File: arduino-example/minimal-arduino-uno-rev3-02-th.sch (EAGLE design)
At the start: 15 parts, among them J1 3x2 M, J3 POWERSUPPLY_DC21MMX, U1 NCP1117ST50T3G, X1 CSTCE16M0V53-R0 16MHZ

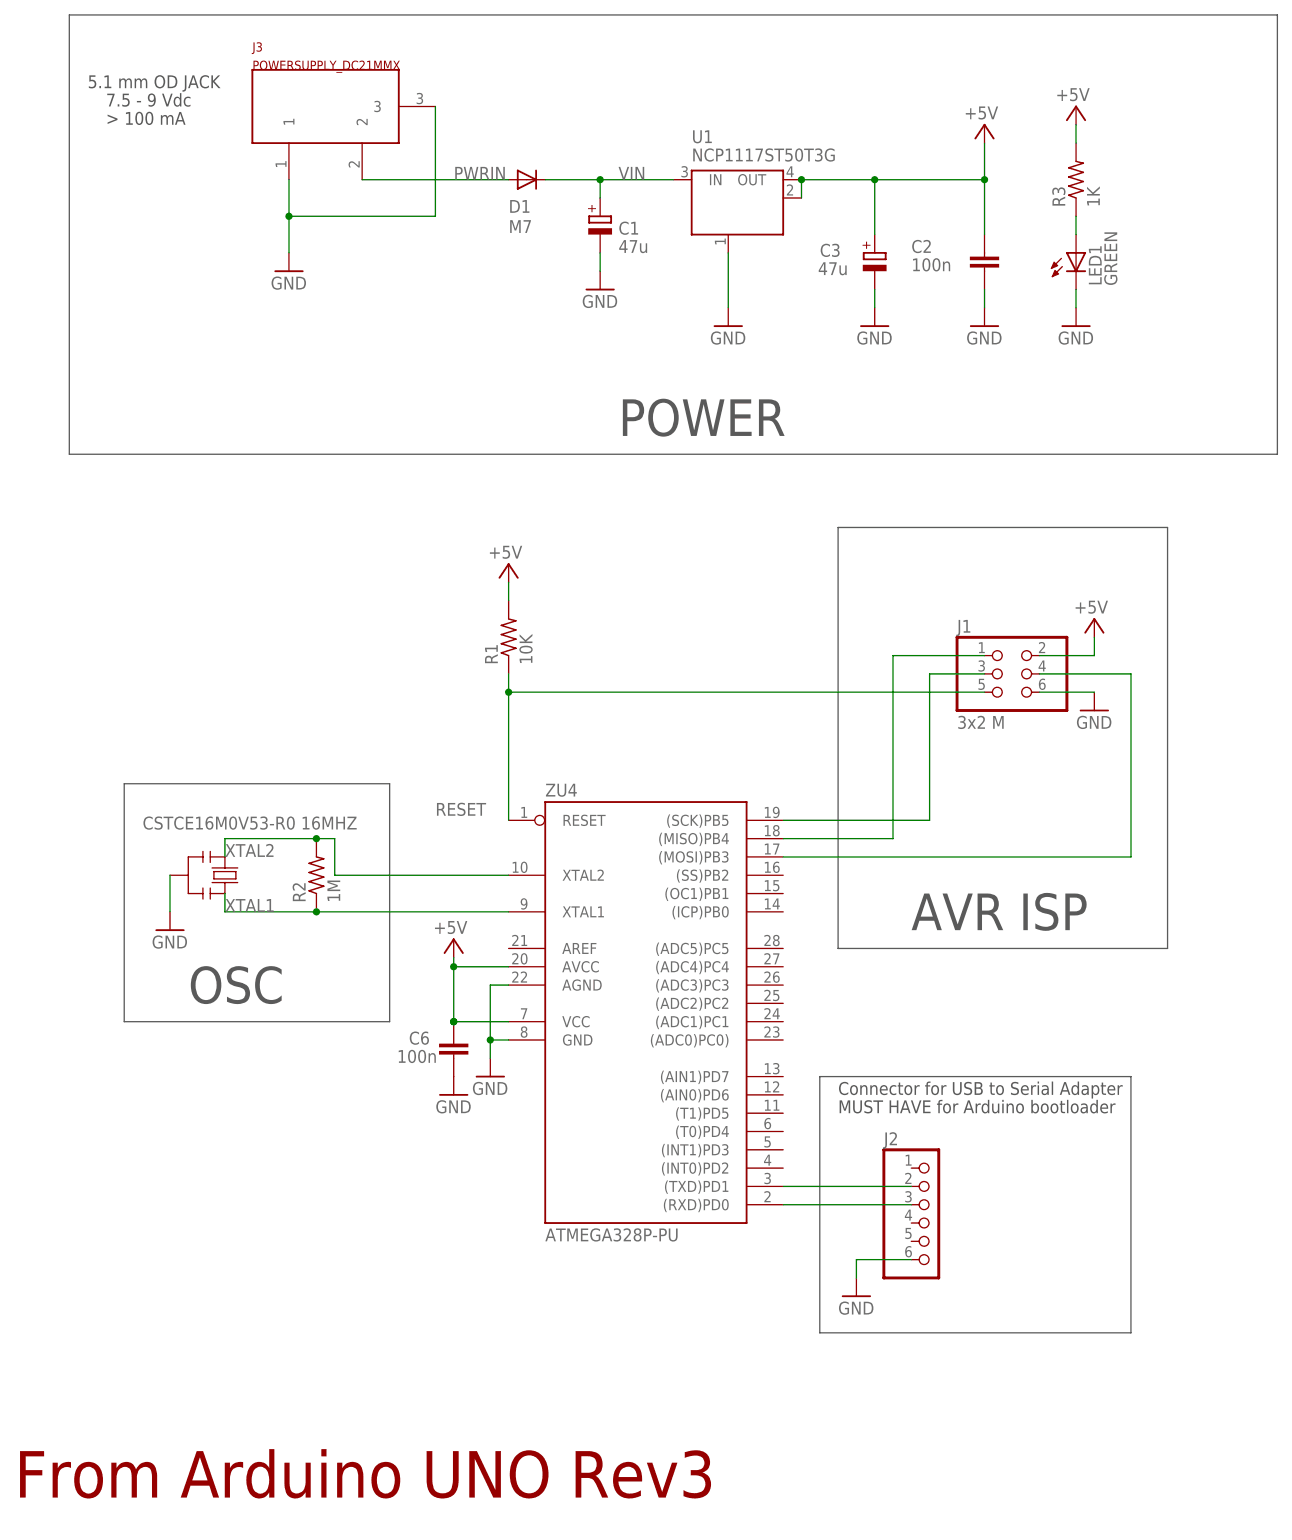
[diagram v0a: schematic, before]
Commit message: Updated minimal arduino board.
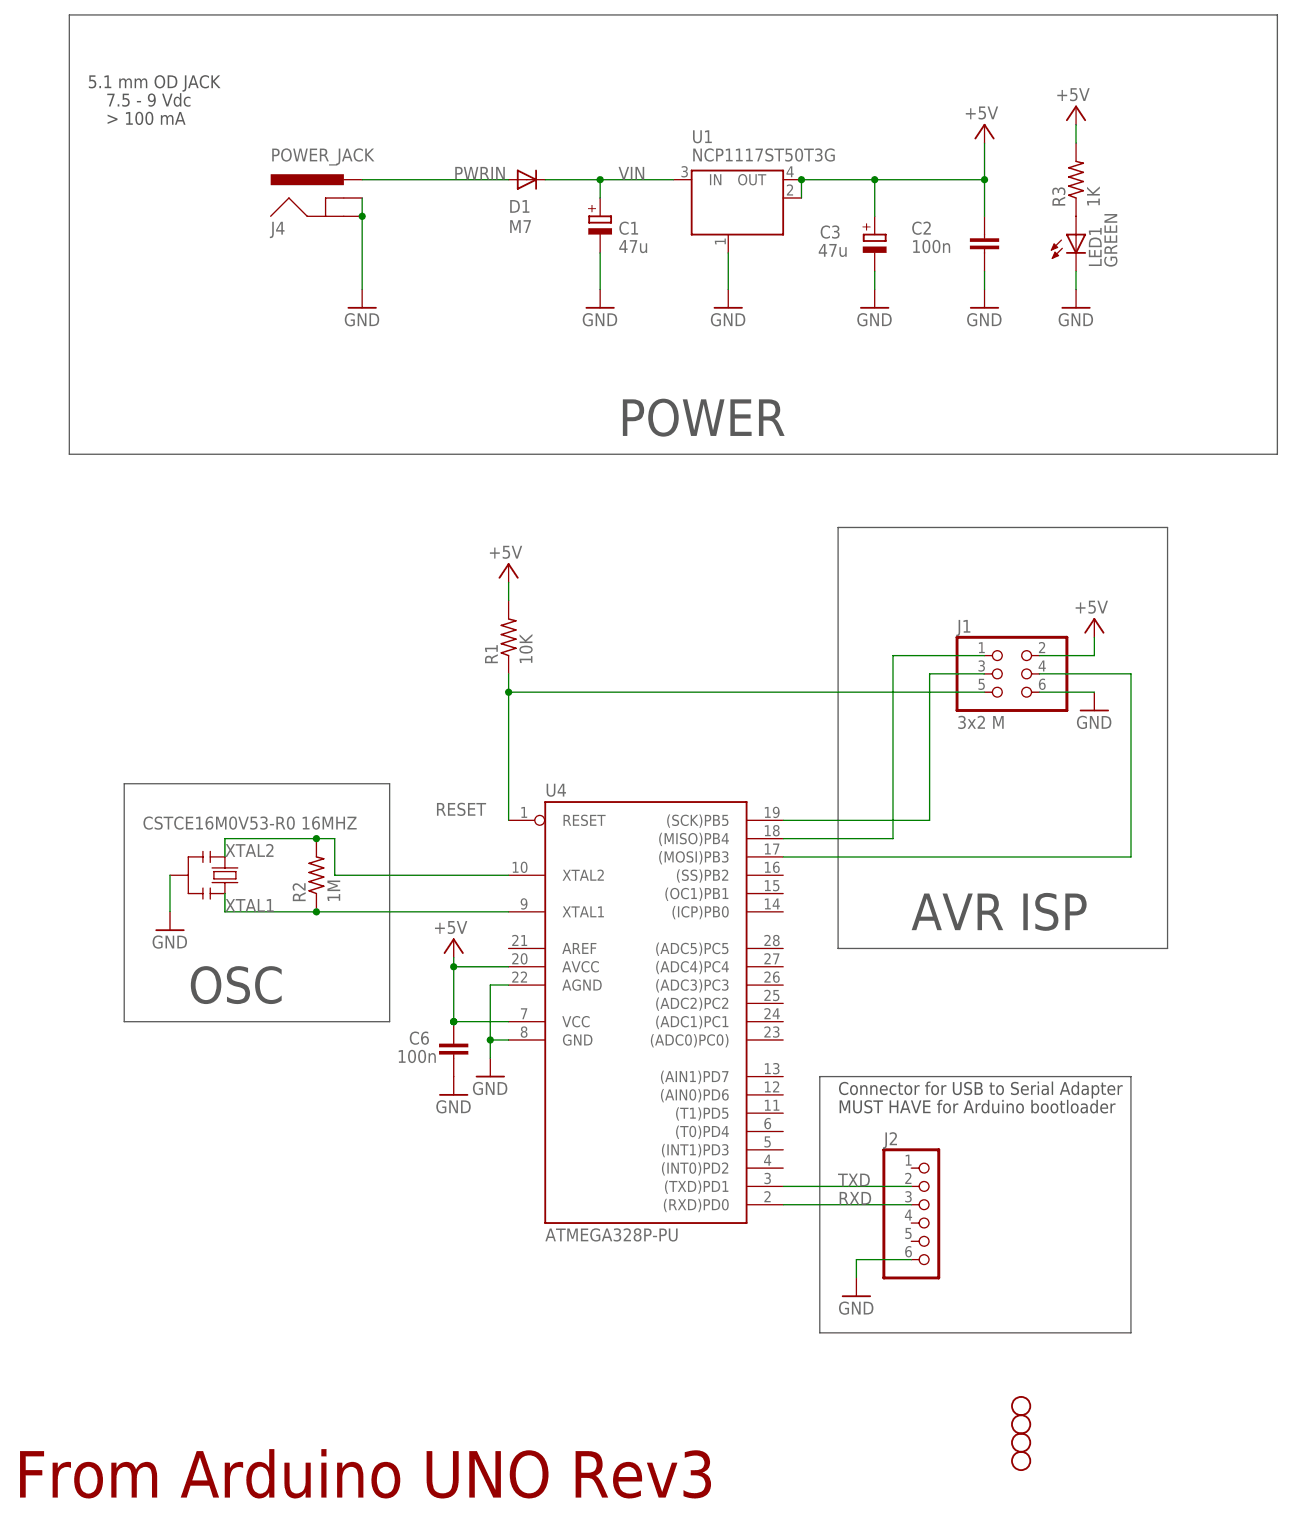
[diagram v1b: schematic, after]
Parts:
- removed J3: POWERSUPPLY_DC21MMX, SmartPrj:POWERSUPPLY_DC21MMX
- added H1, H2, H3, H4: STAND-OFF, SparkFun-Hardware:STAND-OFF
- added J4: POWER_JACK, SparkFun-Connectors:POWER_JACK
- renumbered ZU4 to U4
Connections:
- net N$1 renamed RXD
- net N$2 renamed TXD
- net GND: now also J4.GND, J4.GNDBREAK; no longer J3.1, J3.3
- net PWRIN: now also J4.PWR; no longer J3.2
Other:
- moved on the sheet: C2, C3, LED1
